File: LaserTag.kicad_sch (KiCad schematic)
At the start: 6 parts, among them SW1 SW_SPST, U1 TinyS3_Symbol

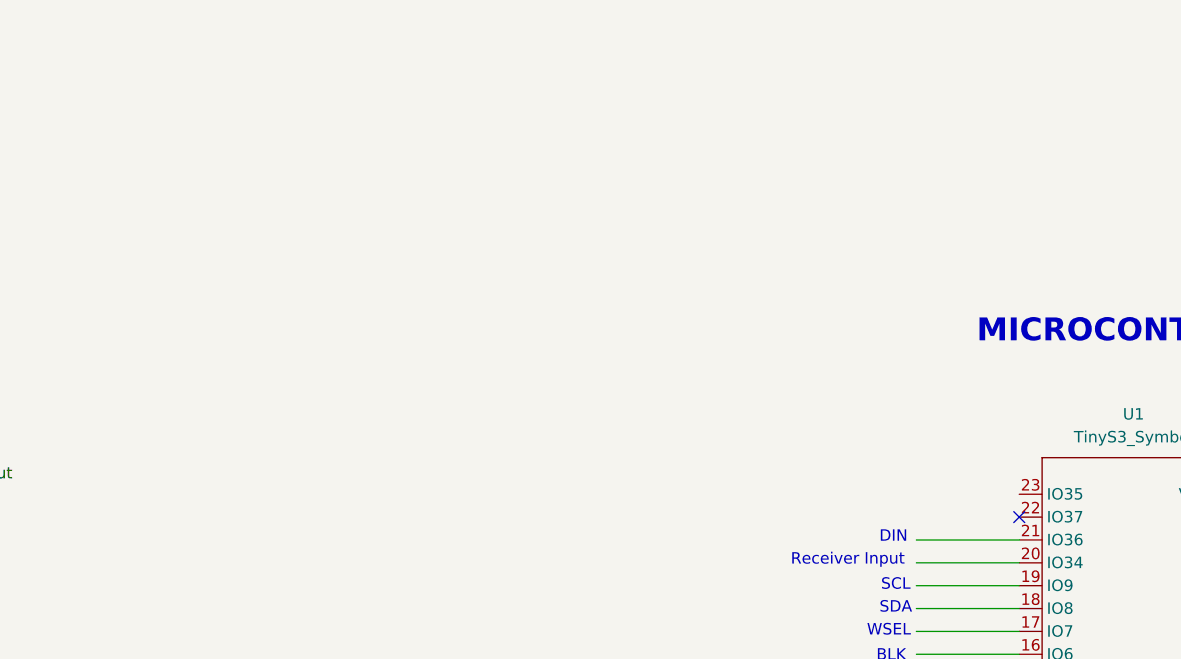
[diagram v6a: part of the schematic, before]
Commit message: included push button in schematic
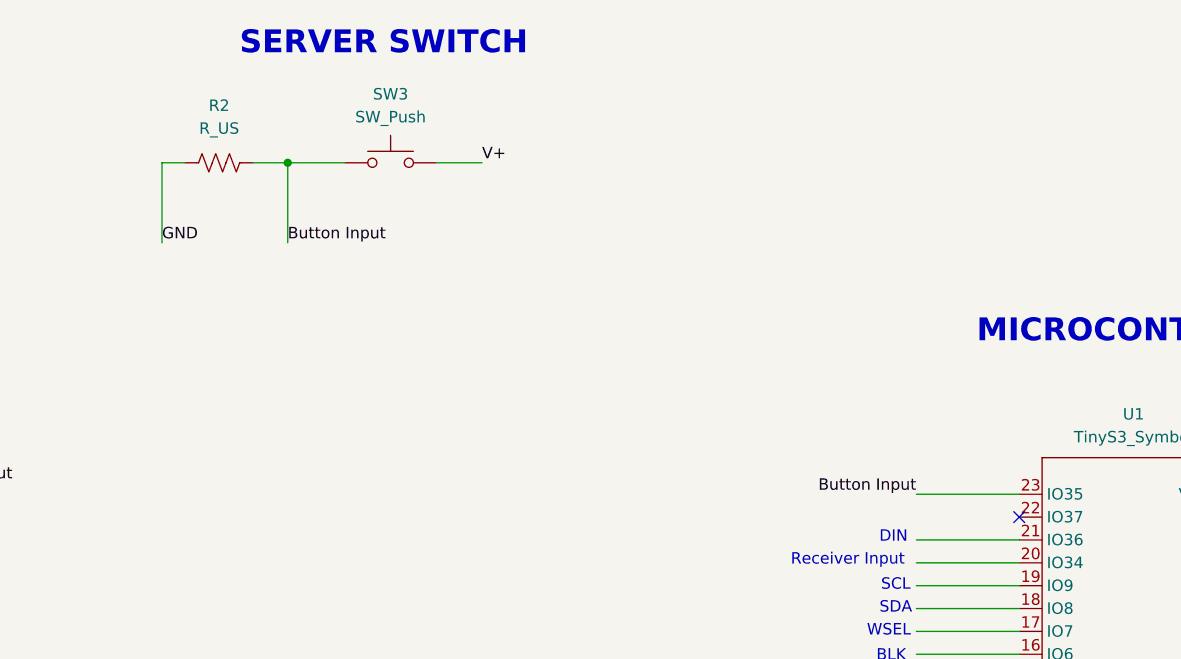
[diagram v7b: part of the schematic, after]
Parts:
- added R2: R_US, symbol Device:R_US
- added SW3: SW_Push, symbol Switch:SW_Push
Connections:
- net GND: now also R2.1
- net V+: now also SW3.2
- net Button Input: now reaches U1.23 (IO35)
- net Button Input: now also R2.2, SW3.1
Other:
- note added: "SERVER SWITCH"

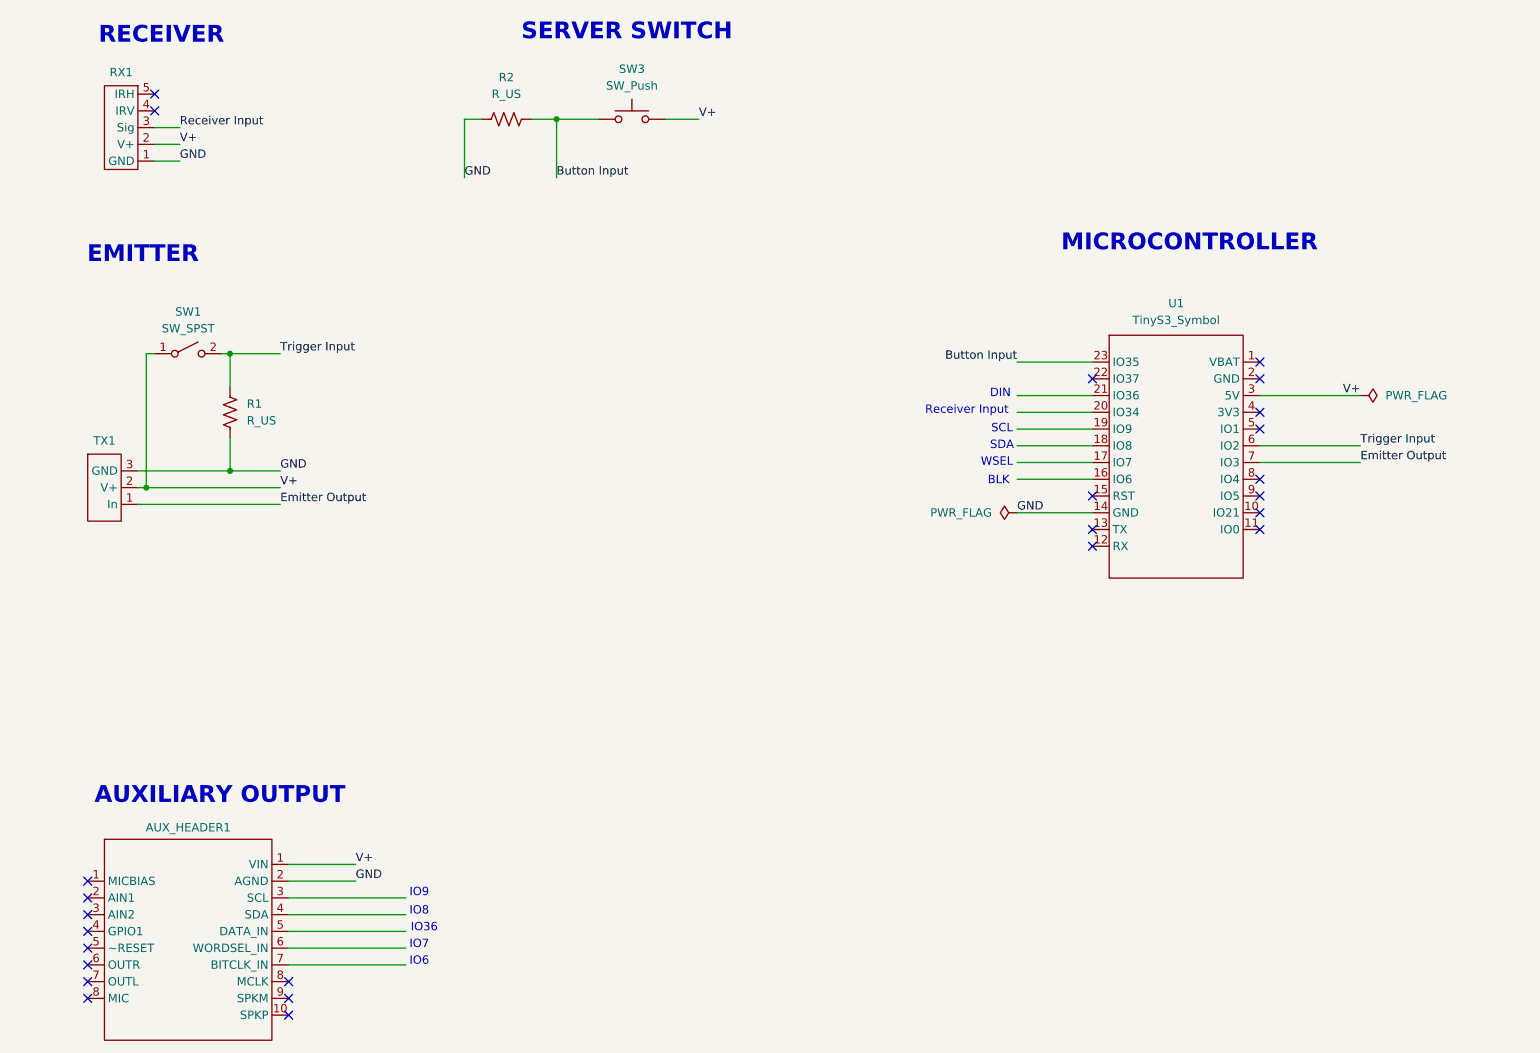
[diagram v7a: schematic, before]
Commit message: Corrected AUX Schematic
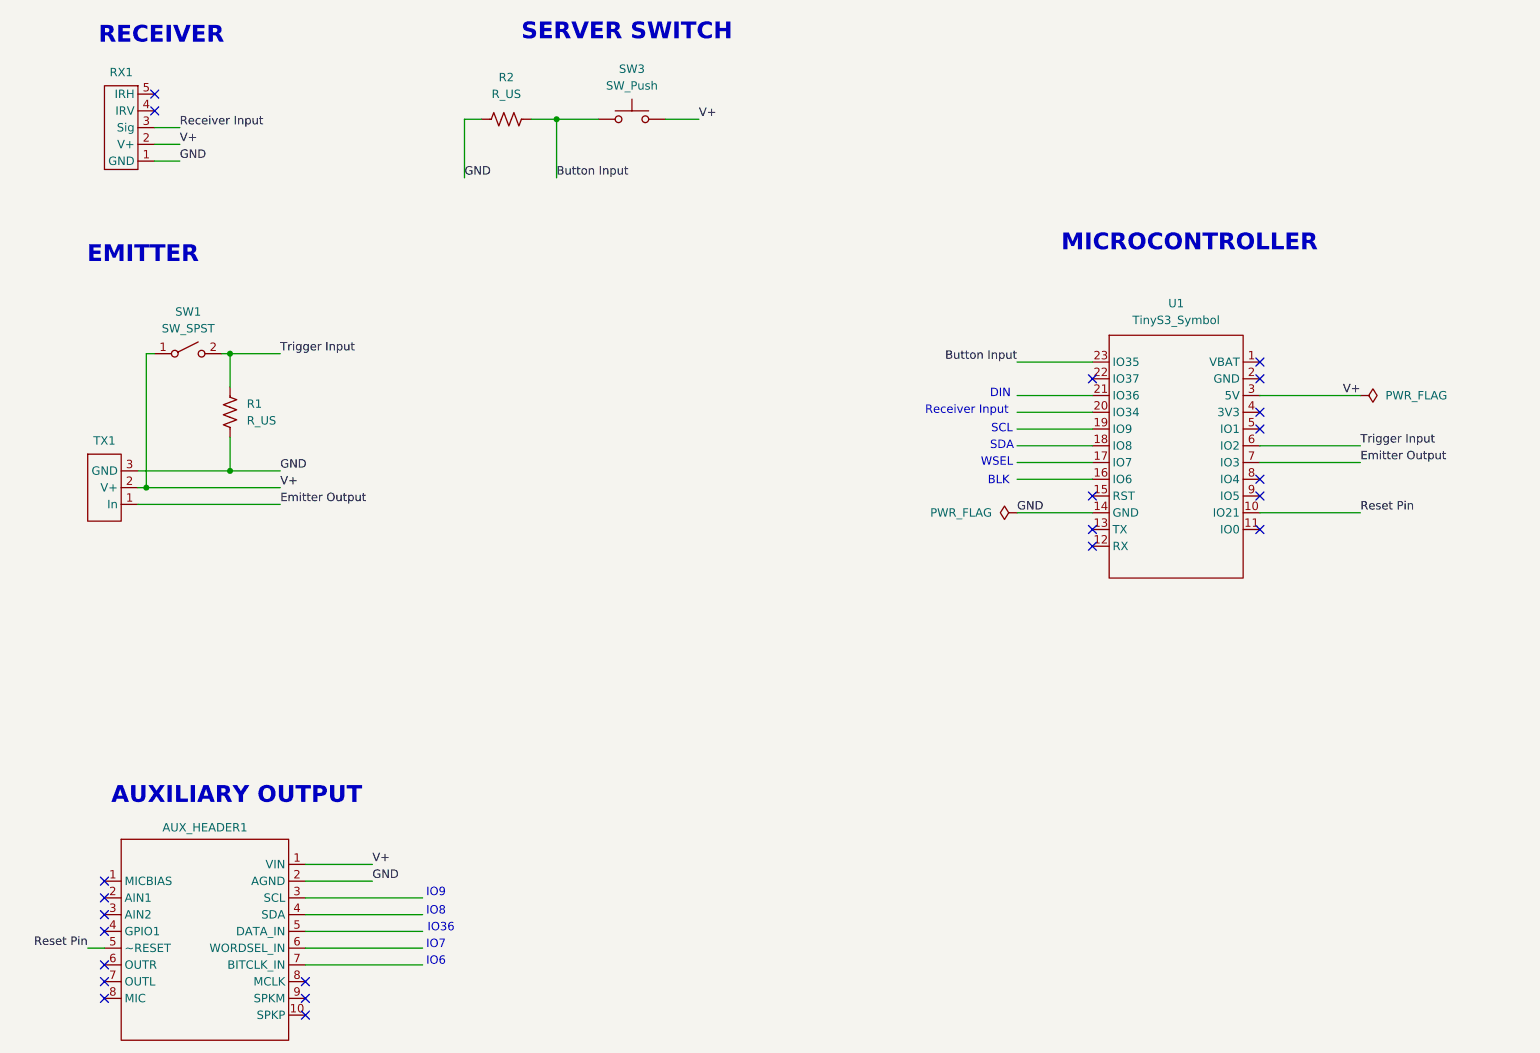
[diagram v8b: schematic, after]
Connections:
- net Reset Pin: now reaches AUX_HEADER1.5 (DATA_IN)
- net Reset Pin: now also U1.10 (IO21)
- no-connect marks 25 -> 23
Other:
- moved on the sheet: AUX_HEADER1
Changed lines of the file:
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@@
 	(text "IO6"
 		(exclude_from_sim no)
-		(at 73.152 158.242 0)
+		(at 75.692 158.242 0)
 		(effects
 			(font
@@
 	(text "IO9"
 		(exclude_from_sim no)
-		(at 73.152 147.828 0)
+		(at 75.692 147.828 0)
 		(effects
 			(font
@@
 	(text "IO8"
 		(exclude_from_sim no)
-		(at 73.152 150.622 0)
+		(at 75.692 150.622 0)
 		(effects
 			(font
@@
 	(text "IO36"
 		(exclude_from_sim no)
-		(at 73.914 153.162 0)
+		(at 76.454 153.162 0)
 		(effects
 			(font
@@
 	(text "IO7"
 		(exclude_from_sim no)
-		(at 73.152 155.702 0)
+		(at 75.692 155.702 0)
 		(effects
 			(font
@@
 	(text "AUXILIARY OUTPUT"
 		(exclude_from_sim no)
-		(at 42.926 133.096 0)
+		(at 45.466 133.096 0)
 		(effects
 			(font
@@
 	)
 	(no_connect
-		(at 22.86 153.67)
+		(at 25.4 153.67)
 	)
 	(no_connect
@@
 	)
 	(no_connect
-		(at 53.34 163.83)
+		(at 55.88 163.83)
 	)
 	(no_connect
@@
 	)
 	(no_connect
-		(at 22.86 148.59)
-	)
-	(no_connect
-		(at 53.34 166.37)
-	)
-	(no_connect
-		(at 22.86 161.29)
+		(at 25.4 148.59)
+	)
+	(no_connect
+		(at 55.88 166.37)
+	)
+	(no_connect
+		(at 25.4 161.29)
 	)
 	(no_connect
@@
 	)
 	(no_connect
-		(at 22.86 151.13)
+		(at 25.4 151.13)
 	)
 	(no_connect
@@
 	)
 	(no_connect
-		(at 200.66 90.17)
-	)
-	(no_connect
 		(at 33.02 29.21)
 	)
 	(no_connect
-		(at 22.86 146.05)
+		(at 25.4 146.05)
 	)
 	(no_connect
@@
 	)
 	(no_connect
-		(at 53.34 161.29)
-	)
-	(no_connect
-		(at 22.86 158.75)
+		(at 55.88 161.29)
+	)
+	(no_connect
+		(at 25.4 158.75)
 	)
 	(no_connect
@@
 	)
 	(no_connect
-		(at 22.86 163.83)
-	)
-	(no_connect
-		(at 22.86 156.21)
-	)
-	(wire
-		(pts
-			(xy 53.34 143.51) (xy 63.5 143.51)
+		(at 25.4 163.83)
+	)
+	(wire
+		(pts
+			(xy 55.88 143.51) (xy 66.04 143.51)
 		)
 		(stroke
@@
 	(wire
 		(pts
-			(xy 53.34 158.75) (xy 71.12 158.75)
+			(xy 55.88 158.75) (xy 73.66 158.75)
 		)
 		(stroke
@@
 	(wire
 		(pts
-			(xy 53.34 153.67) (xy 71.12 153.67)
+			(xy 55.88 153.67) (xy 73.66 153.67)
 		)
 		(stroke
@@
 	(wire
 		(pts
+			(xy 22.86 156.21) (xy 25.4 156.21)
+		)
+		(stroke
+			(width 0)
+			(type default)
+		)
+	)
+	(wire
+		(pts
 			(xy 30.48 83.82) (xy 44.45 83.82)
 		)
@@
 	(wire
 		(pts
-			(xy 53.34 146.05) (xy 63.5 146.05)
+			(xy 55.88 146.05) (xy 66.04 146.05)
 		)
 		(stroke
@@
 	(wire
 		(pts
-			(xy 53.34 151.13) (xy 71.12 151.13)
+			(xy 55.88 151.13) (xy 73.66 151.13)
 		)
 		(stroke
@@
 	(wire
 		(pts
-			(xy 53.34 156.21) (xy 71.12 156.21)
+			(xy 55.88 156.21) (xy 73.66 156.21)
 		)
 		(stroke
@@
 	(wire
 		(pts
-			(xy 53.34 148.59) (xy 71.12 148.59)
+			(xy 55.88 148.59) (xy 73.66 148.59)
 		)
 		(stroke
@@
 		(pts
 			(xy 200.66 80.01) (xy 215.9 80.01)
+		)
+		(stroke
+			(width 0)
+			(type default)
+		)
+	)
+	(wire
+		(pts
+			(xy 200.66 90.17) (xy 215.9 90.17)
 		)
 		(stroke
@@
 		)
 	)
+	(label "Reset Pin"
+		(at 22.86 156.21 180)
+		(effects
+			(font
+				(size 1.27 1.27)
+			)
+			(justify right bottom)
+		)
+	)
 	(label "Trigger Input"
 		(at 52.07 66.04 0)
@@
 	)
 	(label "V+"
-		(at 63.5 143.51 0)
+		(at 66.04 143.51 0)
+		(effects
+			(font
+				(size 1.27 1.27)
+			)
+			(justify left bottom)
+		)
+	)
+	(label "Reset Pin"
+		(at 215.9 90.17 0)
 		(effects
 			(font
@@
 	)
 	(label "GND"
-		(at 63.5 146.05 0)
+		(at 66.04 146.05 0)
 		(effects
 			(font
@@
 	(symbol
 		(lib_id "LaserTagSymbols:LaserTag_Aux_Header")
-		(at 38.1 154.94 0)
+		(at 40.64 154.94 0)
 		(unit 1)
 		(body_style 1)
@@
 		(dnp no)
 		(property "Reference" "AUX_HEADER1"
-			(at 38.1 137.922 0)
+			(at 40.64 137.922 0)
 			(show_name no)
 			(do_not_autoplace no)
@@
 		)
 		(property "Value" ""
-			(at 38.1 137.16 0)
+			(at 40.64 137.16 0)
 			(hide yes)
 			(show_name no)
@@
 		)
 		(property "Footprint" ""
-			(at 38.1 154.94 0)
+			(at 40.64 154.94 0)
 			(hide yes)
 			(show_name no)
@@
 		)
 		(property "Datasheet" ""
-			(at 38.1 154.94 0)
+			(at 40.64 154.94 0)
 			(hide yes)
 			(show_name no)
@@
 		)
 		(property "Description" ""
-			(at 38.1 154.94 0)
-			(hide yes)
-			(show_name no)
+			(at 40.64 154.94 0)
+			(hide yes)
+			(show_name no)
